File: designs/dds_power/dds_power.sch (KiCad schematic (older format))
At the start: 24 parts, among them K1 1.8_3.3, K2 1.8_3.3, K3 1.8_3.3, K4 1.8_3.3, K5 1.8_3.3, K6 1.8_3.3, P1 Vin, P2 12V, P3 12V, P4 12V, P5 12V, P6 12V, P7 12V, U1 QD48T018033

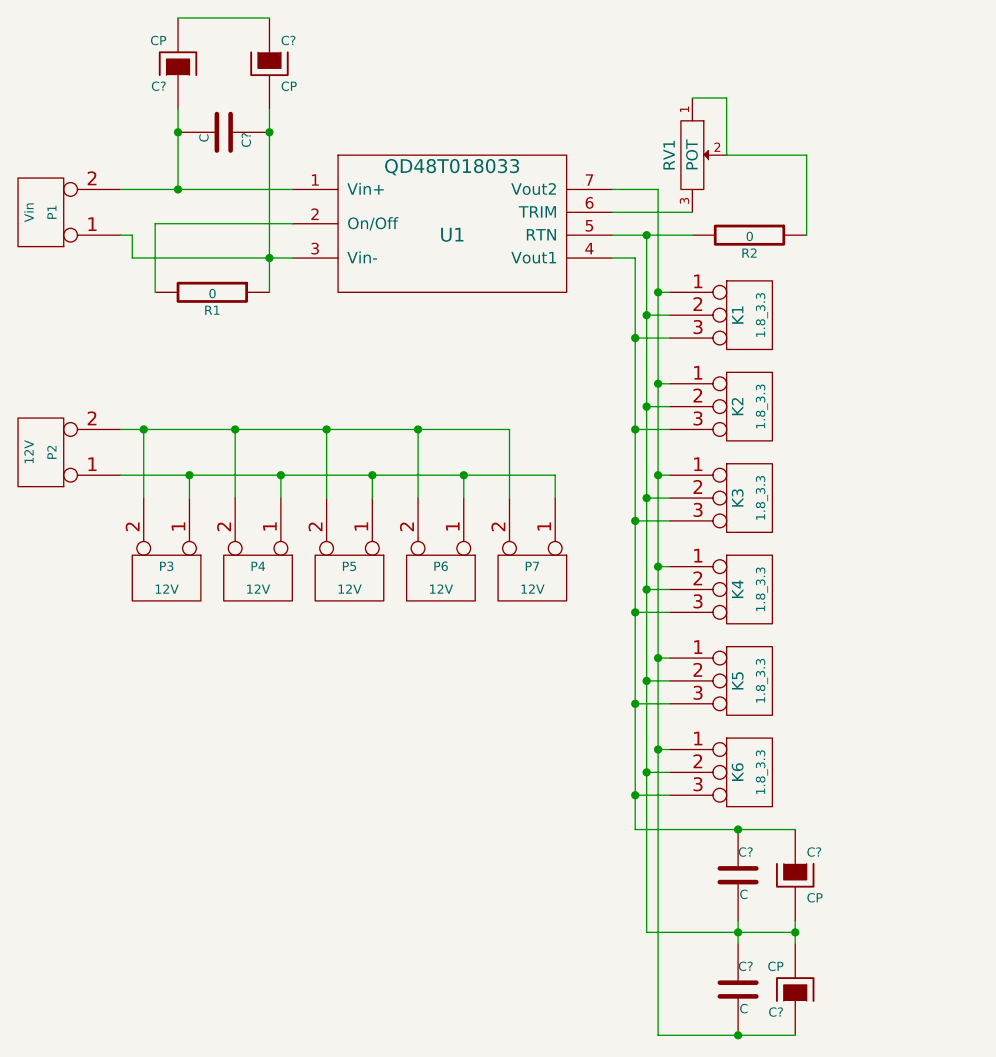
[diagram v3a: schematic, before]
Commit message: [dds_power] ground and net list
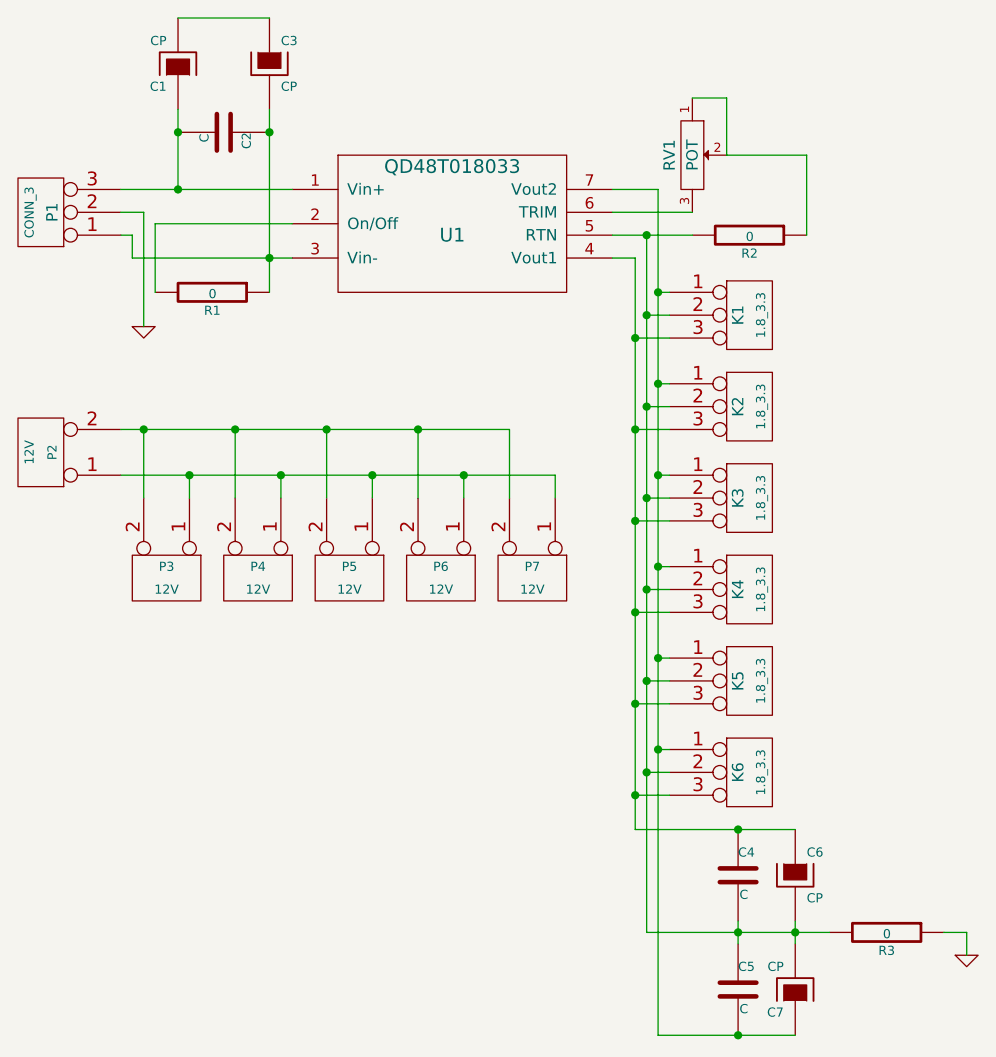
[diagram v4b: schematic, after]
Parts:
- removed P1: Vin, symbol CONN_2
- added P1: CONN_3, cmr_link:3-pins_150mil, symbol CONN_3
- added R3: 0, symbol R
- C1, C3, C6, C7: renamed from C?; footprint (none) -> Capacitors_ThroughHole:C_Radial_D5_L11_P2
- C2, C4, C5: renamed from C?; footprint (none) -> Capacitors_SMD:C_1206
- K1, K2, K3, K4, K5, K6: footprint (none) -> cmr_link:3-pins_150mil
- P2, P3, P4, P5, P6, P7: footprint (none) -> cmr_link:2-pins_150mil
- R1, R2: footprint (none) -> Resistors_SMD:R_0603
- RV1: footprint (none) -> Potentiometers:Potentiometer_Bourns_3005_Angular_ScrewFront
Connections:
- net at C1.1, C2.2, U1.1 (Vin+): now also P1.3 (P3)
- net at C2.1, C3.2, R1.1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: now also P1.1 (P1)
- net at C4.2, C5.1, C6.2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: now also R3.2
- new net GND: P1.2 (PM), R3.1
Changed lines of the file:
@@
-$EndComp
-$Comp
-L CONN_2 P1
-U 1 1 55679718
-P 1450 2550
-F 0 "P1" V 1400 2550 40  0000 C CNN
-F 1 "Vin" V 1500 2550 40  0000 C CNN
-F 2 "" H 1450 2550 60  0001 C CNN
-F 3 "" H 1450 2550 60  0000 C CNN
-	1    1450 2550
-	-1   0    0    1
 $EndComp
 $Comp
@@
 F 0 "R1" V 2280 2900 40  0000 C CNN
 F 1 "0" V 2207 2901 40  0000 C CNN
-F 2 "" V 2130 2900 30  0001 C CNN
+F 2 "Resistors_SMD:R_0603" V 2130 2900 30  0001 C CNN
 F 3 "" H 2200 2900 30  0000 C CNN
 	1    2200 2900
@@
 F 0 "R2" V 4630 2650 40  0000 C CNN
 F 1 "0" V 4557 2651 40  0000 C CNN
-F 2 "" V 4480 2650 30  0001 C CNN
+F 2 "Resistors_SMD:R_0603" V 4480 2650 30  0001 C CNN
 F 3 "" H 4550 2650 30  0000 C CNN
 	1    4550 2650
@@
 F 0 "RV1" H 4300 2200 50  0000 C CNN
 F 1 "POT" H 4300 2300 50  0000 C CNN
-F 2 "" H 4300 2300 60  0001 C CNN
+F 2 "Potentiometers:Potentiometer_Bourns_3005_Angular_ScrewFront" H 4300 2300 60  0001 C CNN
 F 3 "" H 4300 2300 60  0000 C CNN
 	1    4300 2300
@@
 F 0 "P2" V 1400 3600 40  0000 C CNN
 F 1 "12V" V 1500 3600 40  0000 C CNN
-F 2 "" H 1450 3600 60  0001 C CNN
+F 2 "cmr_link:2-pins_150mil" H 1450 3600 60  0001 C CNN
 F 3 "" H 1450 3600 60  0000 C CNN
 	1    1450 3600
@@
 F 0 "P3" V 1950 4150 40  0000 C CNN
 F 1 "12V" V 2050 4150 40  0000 C CNN
-F 2 "" H 2000 4150 60  0001 C CNN
+F 2 "cmr_link:2-pins_150mil" H 2000 4150 60  0001 C CNN
 F 3 "" H 2000 4150 60  0000 C CNN
 	1    2000 4150
@@
 F 0 "P4" V 2350 4150 40  0000 C CNN
 F 1 "12V" V 2450 4150 40  0000 C CNN
-F 2 "" H 2400 4150 60  0001 C CNN
+F 2 "cmr_link:2-pins_150mil" H 2400 4150 60  0001 C CNN
 F 3 "" H 2400 4150 60  0000 C CNN
 	1    2400 4150
@@
 F 0 "P5" V 2750 4150 40  0000 C CNN
 F 1 "12V" V 2850 4150 40  0000 C CNN
-F 2 "" H 2800 4150 60  0001 C CNN
+F 2 "cmr_link:2-pins_150mil" H 2800 4150 60  0001 C CNN
 F 3 "" H 2800 4150 60  0000 C CNN
 	1    2800 4150
@@
 F 0 "P6" V 3150 4150 40  0000 C CNN
 F 1 "12V" V 3250 4150 40  0000 C CNN
-F 2 "" H 3200 4150 60  0001 C CNN
+F 2 "cmr_link:2-pins_150mil" H 3200 4150 60  0001 C CNN
 F 3 "" H 3200 4150 60  0000 C CNN
 	1    3200 4150
@@
 F 0 "P7" V 3550 4150 40  0000 C CNN
 F 1 "12V" V 3650 4150 40  0000 C CNN
-F 2 "" H 3600 4150 60  0001 C CNN
+F 2 "cmr_link:2-pins_150mil" H 3600 4150 60  0001 C CNN
 F 3 "" H 3600 4150 60  0000 C CNN
 	1    3600 4150
@@
 F 0 "K1" V 4500 3000 50  0000 C CNN
 F 1 "1.8_3.3" V 4600 3000 40  0000 C CNN
-F 2 "" H 4550 3000 60  0001 C CNN
+F 2 "cmr_link:3-pins_150mil" H 4550 3000 60  0001 C CNN
 F 3 "" H 4550 3000 60  0000 C CNN
 	1    4550 3000
@@
 F 0 "K2" V 4500 3400 50  0000 C CNN
 F 1 "1.8_3.3" V 4600 3400 40  0000 C CNN
-F 2 "" H 4550 3400 60  0001 C CNN
+F 2 "cmr_link:3-pins_150mil" H 4550 3400 60  0001 C CNN
 F 3 "" H 4550 3400 60  0000 C CNN
 	1    4550 3400
@@
 F 0 "K3" V 4500 3800 50  0000 C CNN
 F 1 "1.8_3.3" V 4600 3800 40  0000 C CNN
-F 2 "" H 4550 3800 60  0001 C CNN
+F 2 "cmr_link:3-pins_150mil" H 4550 3800 60  0001 C CNN
 F 3 "" H 4550 3800 60  0000 C CNN
 	1    4550 3800
@@
 F 0 "K4" V 4500 4200 50  0000 C CNN
 F 1 "1.8_3.3" V 4600 4200 40  0000 C CNN
-F 2 "" H 4550 4200 60  0001 C CNN
+F 2 "cmr_link:3-pins_150mil" H 4550 4200 60  0001 C CNN
 F 3 "" H 4550 4200 60  0000 C CNN
 	1    4550 4200
@@
 F 0 "K5" V 4500 4600 50  0000 C CNN
 F 1 "1.8_3.3" V 4600 4600 40  0000 C CNN
-F 2 "" H 4550 4600 60  0001 C CNN
+F 2 "cmr_link:3-pins_150mil" H 4550 4600 60  0001 C CNN
 F 3 "" H 4550 4600 60  0000 C CNN
 	1    4550 4600
@@
 F 0 "K6" V 4500 5000 50  0000 C CNN
 F 1 "1.8_3.3" V 4600 5000 40  0000 C CNN
-F 2 "" H 4550 5000 60  0001 C CNN
+F 2 "cmr_link:3-pins_150mil" H 4550 5000 60  0001 C CNN
 F 3 "" H 4550 5000 60  0000 C CNN
 	1    4550 5000
@@
 $EndComp
 $Comp
-L C C?
+L C C2
 U 1 1 55687ADF
 P 2250 2200
-F 0 "C?" H 2250 2300 40  0000 L CNN
+F 0 "C2" H 2250 2300 40  0000 L CNN
 F 1 "C" H 2256 2115 40  0000 L CNN
-F 2 "" H 2288 2050 30  0000 C CNN
+F 2 "Capacitors_SMD:C_1206" H 2288 2050 30  0001 C CNN
 F 3 "" H 2250 2200 60  0000 C CNN
 	1    2250 2200
@@
 $EndComp
 $Comp
-L C C?
+L C C4
 U 1 1 55687E96
 P 4500 5450
-F 0 "C?" H 4500 5550 40  0000 L CNN
+F 0 "C4" H 4500 5550 40  0000 L CNN
 F 1 "C" H 4506 5365 40  0000 L CNN
-F 2 "" H 4538 5300 30  0000 C CNN
+F 2 "Capacitors_SMD:C_1206" H 4538 5300 30  0001 C CNN
 F 3 "" H 4500 5450 60  0000 C CNN
 	1    4500 5450
@@
 $EndComp
 $Comp
-L C C?
+L C C5
 U 1 1 55687EED
 P 4500 5950
-F 0 "C?" H 4500 6050 40  0000 L CNN
+F 0 "C5" H 4500 6050 40  0000 L CNN
 F 1 "C" H 4506 5865 40  0000 L CNN
-F 2 "" H 4538 5800 30  0000 C CNN
+F 2 "Capacitors_SMD:C_1206" H 4538 5800 30  0001 C CNN
 F 3 "" H 4500 5950 60  0000 C CNN
 	1    4500 5950
@@
 $EndComp
 $Comp
-L CP C?
+L CP C7
 U 1 1 556883ED
 P 4750 5950
-F 0 "C?" H 4800 6050 40  0000 L CNN
+F 0 "C7" H 4800 6050 40  0000 L CNN
 F 1 "CP" H 4800 5850 40  0000 L CNN
-F 2 "" H 4850 5800 30  0000 C CNN
+F 2 "Capacitors_ThroughHole:C_Radial_D5_L11_P2" H 4850 5800 30  0001 C CNN
 F 3 "" H 4750 5950 300 0000 C CNN
 	1    4750 5950
@@
 $EndComp
 $Comp
-L CP C?
+L CP C6
 U 1 1 556883C0
 P 4750 5450
-F 0 "C?" H 4800 5550 40  0000 L CNN
+F 0 "C6" H 4800 5550 40  0000 L CNN
 F 1 "CP" H 4800 5350 40  0000 L CNN
-F 2 "" H 4850 5300 30  0000 C CNN
+F 2 "Capacitors_ThroughHole:C_Radial_D5_L11_P2" H 4850 5300 30  0001 C CNN
 F 3 "" H 4750 5450 300 0000 C CNN
 	1    4750 5450
@@
 $EndComp
 Wire Wire Line
-	2550 2450 1800 2450
+	1800 2450 2550 2450
 Wire Wire Line
 	1800 2650 1850 2650
@@
 Connection ~ 4500 5250
 Wire Wire Line
-	4500 5750 4500 5650
+	4500 5650 4500 5750
 Wire Wire Line
 	4750 5650 4750 5750
@@
 Connection ~ 4500 6150
 Wire Wire Line
-	4100 5700 4750 5700
+	4100 5700 4900 5700
 Connection ~ 4500 5700
 Connection ~ 4750 5700
 Connection ~ 4100 5000
 $Comp
-L CP C?
+L CP C1
 U 1 1 55688DD5
 P 2050 1900
-F 0 "C?" H 2100 2000 40  0000 L CNN
+F 0 "C1" H 2100 2000 40  0000 L CNN
 F 1 "CP" H 2100 1800 40  0000 L CNN
-F 2 "" H 2150 1750 30  0000 C CNN
+F 2 "Capacitors_ThroughHole:C_Radial_D5_L11_P2" H 2150 1750 30  0001 C CNN
 F 3 "" H 2050 1900 300 0000 C CNN
 	1    2050 1900
@@
 $EndComp
 $Comp
-L CP C?
+L CP C3
 U 1 1 556890A2
 P 2450 1900
-F 0 "C?" H 2500 2000 40  0000 L CNN
+F 0 "C3" H 2500 2000 40  0000 L CNN
 F 1 "CP" H 2500 1800 40  0000 L CNN
-F 2 "" H 2550 1750 30  0000 C CNN
+F 2 "Capacitors_ThroughHole:C_Radial_D5_L11_P2" H 2550 1750 30  0001 C CNN
 F 3 "" H 2450 1900 300 0000 C CNN
 	1    2450 1900
@@
 Wire Wire Line
 	2450 1700 2050 1700
+$Comp
+L CONN_3 P1
+U 1 1 55689EDE
+P 1450 2550
+F 0 "P1" V 1400 2550 50  0000 C CNN
+F 1 "CONN_3" V 1500 2550 40  0000 C CNN
+F 2 "cmr_link:3-pins_150mil" H 1450 2550 60  0001 C CNN
+F 3 "" H 1450 2550 60  0000 C CNN
+	1    1450 2550
+	-1   0    0    1
+$EndComp
+$Comp
+L GND #PWR01
+U 1 1 5568A308
+P 1900 3050
+F 0 "#PWR01" H 1900 3050 30  0001 C CNN
+F 1 "GND" H 1900 2980 30  0001 C CNN
+F 2 "" H 1900 3050 60  0000 C CNN
+F 3 "" H 1900 3050 60  0000 C CNN
+	1    1900 3050
+	1    0    0    -1
+$EndComp
+Wire Wire Line
+	1900 3050 1900 2550
+Wire Wire Line
+	1900 2550 1800 2550
+$Comp
+L GND #PWR02
+U 1 1 5568A57C
+P 5500 5800
+F 0 "#PWR02" H 5500 5800 30  0001 C CNN
+F 1 "GND" H 5500 5730 30  0001 C CNN
+F 2 "" H 5500 5800 60  0000 C CNN
+F 3 "" H 5500 5800 60  0000 C CNN
+	1    5500 5800
+	1    0    0    -1
+$EndComp
+$Comp
+L R R3
+U 1 1 5568A5A8
+P 5150 5700
+F 0 "R3" V 5230 5700 40  0000 C CNN
+F 1 "0" V 5157 5701 40  0000 C CNN
+F 2 "" V 5080 5700 30  0001 C CNN
+F 3 "" H 5150 5700 30  0000 C CNN
+	1    5150 5700
+	0    1    1    0
+$EndComp
+Wire Wire Line
+	5500 5800 5500 5700
+Wire Wire Line
+	5500 5700 5400 5700
 $EndSCHEMATC

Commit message: [dds_power] pcb
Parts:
- R3: footprint (none) -> Resistors_SMD:R_0603
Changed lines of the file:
@@
 F 0 "R3" V 5230 5700 40  0000 C CNN
 F 1 "0" V 5157 5701 40  0000 C CNN
-F 2 "" V 5080 5700 30  0001 C CNN
+F 2 "Resistors_SMD:R_0603" V 5080 5700 30  0001 C CNN
 F 3 "" H 5150 5700 30  0000 C CNN
 	1    5150 5700

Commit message: [dds_power] tweak
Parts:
- K1, K2, K3, K4, K5, K6: value 1.8_3.3 -> 3.3_1.8
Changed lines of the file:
@@
 P 4550 3000
 F 0 "K1" V 4500 3000 50  0000 C CNN
-F 1 "1.8_3.3" V 4600 3000 40  0000 C CNN
+F 1 "3.3_1.8" V 4600 3000 40  0000 C CNN
 F 2 "cmr_link:3-pins_150mil" H 4550 3000 60  0001 C CNN
 F 3 "" H 4550 3000 60  0000 C CNN
@@
 P 4550 3400
 F 0 "K2" V 4500 3400 50  0000 C CNN
-F 1 "1.8_3.3" V 4600 3400 40  0000 C CNN
+F 1 "3.3_1.8" V 4600 3400 40  0000 C CNN
 F 2 "cmr_link:3-pins_150mil" H 4550 3400 60  0001 C CNN
 F 3 "" H 4550 3400 60  0000 C CNN
@@
 P 4550 3800
 F 0 "K3" V 4500 3800 50  0000 C CNN
-F 1 "1.8_3.3" V 4600 3800 40  0000 C CNN
+F 1 "3.3_1.8" V 4600 3800 40  0000 C CNN
 F 2 "cmr_link:3-pins_150mil" H 4550 3800 60  0001 C CNN
 F 3 "" H 4550 3800 60  0000 C CNN
@@
 P 4550 4200
 F 0 "K4" V 4500 4200 50  0000 C CNN
-F 1 "1.8_3.3" V 4600 4200 40  0000 C CNN
+F 1 "3.3_1.8" V 4600 4200 40  0000 C CNN
 F 2 "cmr_link:3-pins_150mil" H 4550 4200 60  0001 C CNN
 F 3 "" H 4550 4200 60  0000 C CNN
@@
 P 4550 4600
 F 0 "K5" V 4500 4600 50  0000 C CNN
-F 1 "1.8_3.3" V 4600 4600 40  0000 C CNN
+F 1 "3.3_1.8" V 4600 4600 40  0000 C CNN
 F 2 "cmr_link:3-pins_150mil" H 4550 4600 60  0001 C CNN
 F 3 "" H 4550 4600 60  0000 C CNN
@@
 P 4550 5000
 F 0 "K6" V 4500 5000 50  0000 C CNN
-F 1 "1.8_3.3" V 4600 5000 40  0000 C CNN
+F 1 "3.3_1.8" V 4600 5000 40  0000 C CNN
 F 2 "cmr_link:3-pins_150mil" H 4550 5000 60  0001 C CNN
 F 3 "" H 4550 5000 60  0000 C CNN

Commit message: [designs/dds_power] update to kicad 4.0, add missing mount hole
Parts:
- C1, C3, C6, C7: symbol CP -> CP-RESCUE-dds_power
- C2, C4, C5: symbol C -> C-RESCUE-dds_power
- R1, R2, R3: symbol R -> R-RESCUE-dds_power
- RV1: symbol POT -> POT-RESCUE-dds_power
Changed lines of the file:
@@
 EESchema Schematic File Version 2
+LIBS:dds_power-rescue
 LIBS:power
 LIBS:device
@@
 $EndComp
 $Comp
-L R R1
+L R-RESCUE-dds_power R1
 U 1 1 55679800
 P 2200 2900
@@
 $EndComp
 $Comp
-L R R2
+L R-RESCUE-dds_power R2
 U 1 1 55679B76
 P 4550 2650
@@
 $EndComp
 $Comp
-L POT RV1
+L POT-RESCUE-dds_power RV1
 U 1 1 55679BD9
 P 4300 2300
@@
 $EndComp
 $Comp
-L C C2
+L C-RESCUE-dds_power C2
 U 1 1 55687ADF
 P 2250 2200
@@
 $EndComp
 $Comp
-L C C4
+L C-RESCUE-dds_power C4
 U 1 1 55687E96
 P 4500 5450
@@
 $EndComp
 $Comp
-L C C5
+L C-RESCUE-dds_power C5
 U 1 1 55687EED
 P 4500 5950
@@
 $EndComp
 $Comp
-L CP C7
+L CP-RESCUE-dds_power C7
 U 1 1 556883ED
 P 4750 5950
@@
 $EndComp
 $Comp
-L CP C6
+L CP-RESCUE-dds_power C6
 U 1 1 556883C0
 P 4750 5450
@@
 Connection ~ 4100 5000
 $Comp
-L CP C1
+L CP-RESCUE-dds_power C1
 U 1 1 55688DD5
 P 2050 1900
@@
 $EndComp
 $Comp
-L CP C3
+L CP-RESCUE-dds_power C3
 U 1 1 556890A2
 P 2450 1900
@@
 $EndComp
 $Comp
-L GND #PWR01
+L GND-RESCUE-dds_power #PWR01
 U 1 1 5568A308
 P 1900 3050
@@
 	1900 2550 1800 2550
 $Comp
-L GND #PWR02
+L GND-RESCUE-dds_power #PWR02
 U 1 1 5568A57C
 P 5500 5800
@@
 $EndComp
 $Comp
-L R R3
+L R-RESCUE-dds_power R3
 U 1 1 5568A5A8
 P 5150 5700
